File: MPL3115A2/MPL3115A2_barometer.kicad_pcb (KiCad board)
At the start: 2 copper layers, 9.4 x 9.1 mm, 4 parts, among them U1 MPL3115A2

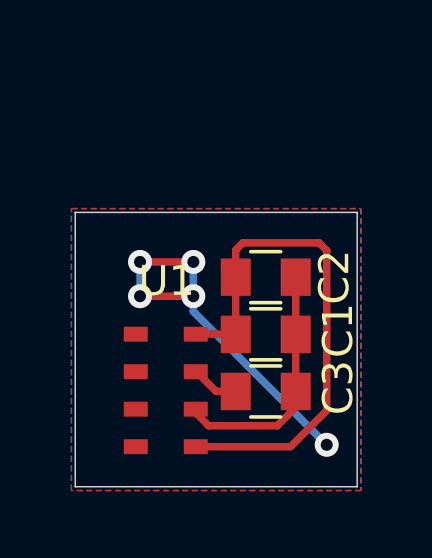
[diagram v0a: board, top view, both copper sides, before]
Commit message: add test point for CAP pin
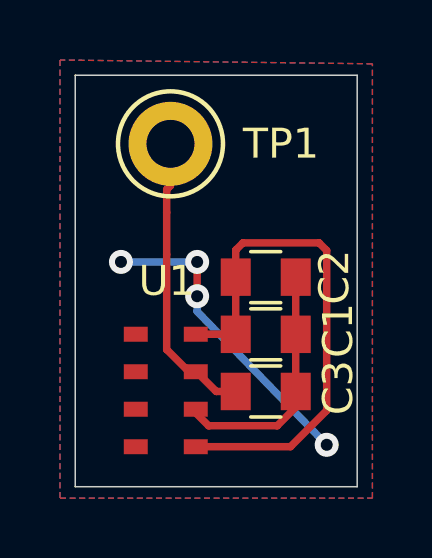
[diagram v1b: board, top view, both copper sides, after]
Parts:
- added TP1: TestPoint, TestPoint:TestPoint_Keystone_5010-5014_Multipurpose, F.Cu at (141.0, 82.0)
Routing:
- net Net-(C3-Pad1): track 1.60 -> 9.79 mm
- net GND: track 21.0 -> 18.7 mm, vias 5 -> 4
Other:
- board size 9.4 x 9.1 mm -> 9.4 x 13.7 mm
